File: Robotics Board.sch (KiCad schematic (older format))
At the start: 0 parts

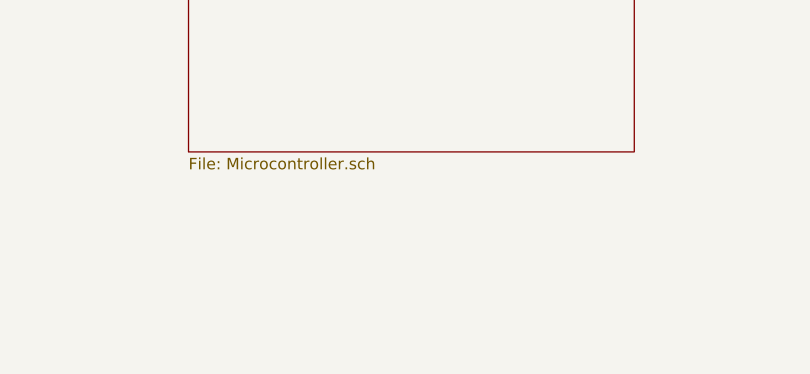
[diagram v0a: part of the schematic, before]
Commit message: Changed the footprint of the PIC to the correct one. Changed the layout of the development area, to be more suited for development Changed the layout of the reset button and programmer header. The programmer header now needs to be a 90deg header, for the pickit3 to fit Added components for the mounting holes and OSHW logos.
Signed-off-by: Kolijn Wolfaardt <kolijn.wolfaardt2gmail.com>
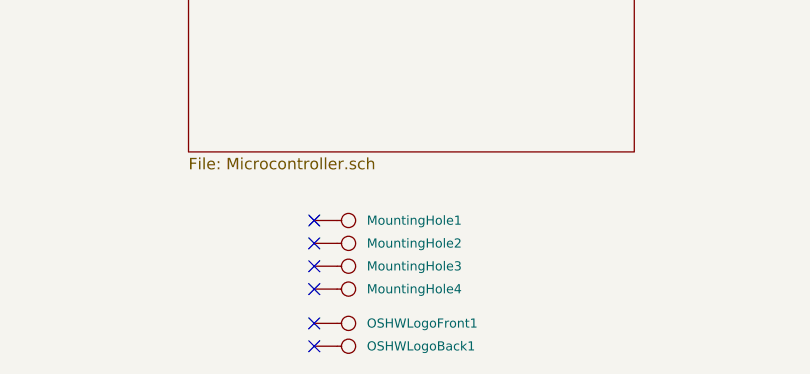
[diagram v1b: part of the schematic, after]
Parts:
- added MountingHole1, MountingHole2, MountingHole3, MountingHole4, OSHWLogoBack1, OSHWLogoFront1: CONN_1, symbol CONN_1
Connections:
- no-connect marks 0 -> 6
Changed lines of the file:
@@
 LIBS:pic18f4550
 LIBS:l293
-LIBS:dp_devices
 LIBS:Robotics Board-cache
 EELAYER 27 0
@@
 Sheet 1 6
 Title ""
-Date "12 feb 2014"
+Date "18 apr 2014"
 Rev ""
 Comp ""
@@
 F1 "PrototypeArea.sch" 50
 $EndSheet
+$Comp
+L CONN_1 MountingHole1
+U 1 1 53513413
+P 5300 6400
+F 0 "MountingHole1" H 5380 6400 40  0000 L CNN
+F 1 "CONN_1" H 5300 6455 30  0001 C CNN
+F 2 "" H 5300 6400 60  0000 C CNN
+F 3 "" H 5300 6400 60  0000 C CNN
+	1    5300 6400
+	1    0    0    -1
+$EndComp
+$Comp
+L CONN_1 MountingHole2
+U 1 1 53513653
+P 5300 6500
+F 0 "MountingHole2" H 5380 6500 40  0000 L CNN
+F 1 "CONN_1" H 5300 6555 30  0001 C CNN
+F 2 "" H 5300 6500 60  0000 C CNN
+F 3 "" H 5300 6500 60  0000 C CNN
+	1    5300 6500
+	1    0    0    -1
+$EndComp
+$Comp
+L CONN_1 MountingHole3
+U 1 1 53513659
+P 5300 6600
+F 0 "MountingHole3" H 5380 6600 40  0000 L CNN
+F 1 "CONN_1" H 5300 6655 30  0001 C CNN
+F 2 "" H 5300 6600 60  0000 C CNN
+F 3 "" H 5300 6600 60  0000 C CNN
+	1    5300 6600
+	1    0    0    -1
+$EndComp
+$Comp
+L CONN_1 MountingHole4
+U 1 1 5351365F
+P 5300 6700
+F 0 "MountingHole4" H 5380 6700 40  0000 L CNN
+F 1 "CONN_1" H 5300 6755 30  0001 C CNN
+F 2 "" H 5300 6700 60  0000 C CNN
+F 3 "" H 5300 6700 60  0000 C CNN
+	1    5300 6700
+	1    0    0    -1
+$EndComp
+$Comp
+L CONN_1 OSHWLogoFront1
+U 1 1 53513665
+P 5300 6850
+F 0 "OSHWLogoFront1" H 5380 6850 40  0000 L CNN
+F 1 "CONN_1" H 5300 6905 30  0001 C CNN
+F 2 "" H 5300 6850 60  0000 C CNN
+F 3 "" H 5300 6850 60  0000 C CNN
+	1    5300 6850
+	1    0    0    -1
+$EndComp
+$Comp
+L CONN_1 OSHWLogoBack1
+U 1 1 5351372F
+P 5300 6950
+F 0 "OSHWLogoBack1" H 5380 6950 40  0000 L CNN
+F 1 "CONN_1" H 5300 7005 30  0001 C CNN
+F 2 "" H 5300 6950 60  0000 C CNN
+F 3 "" H 5300 6950 60  0000 C CNN
+	1    5300 6950
+	1    0    0    -1
+$EndComp
+NoConn ~ 5150 6950
+NoConn ~ 5150 6850
+NoConn ~ 5150 6700
+NoConn ~ 5150 6600
+NoConn ~ 5150 6500
+NoConn ~ 5150 6400
 $EndSCHEMATC
